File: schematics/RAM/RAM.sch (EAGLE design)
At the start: 31 parts

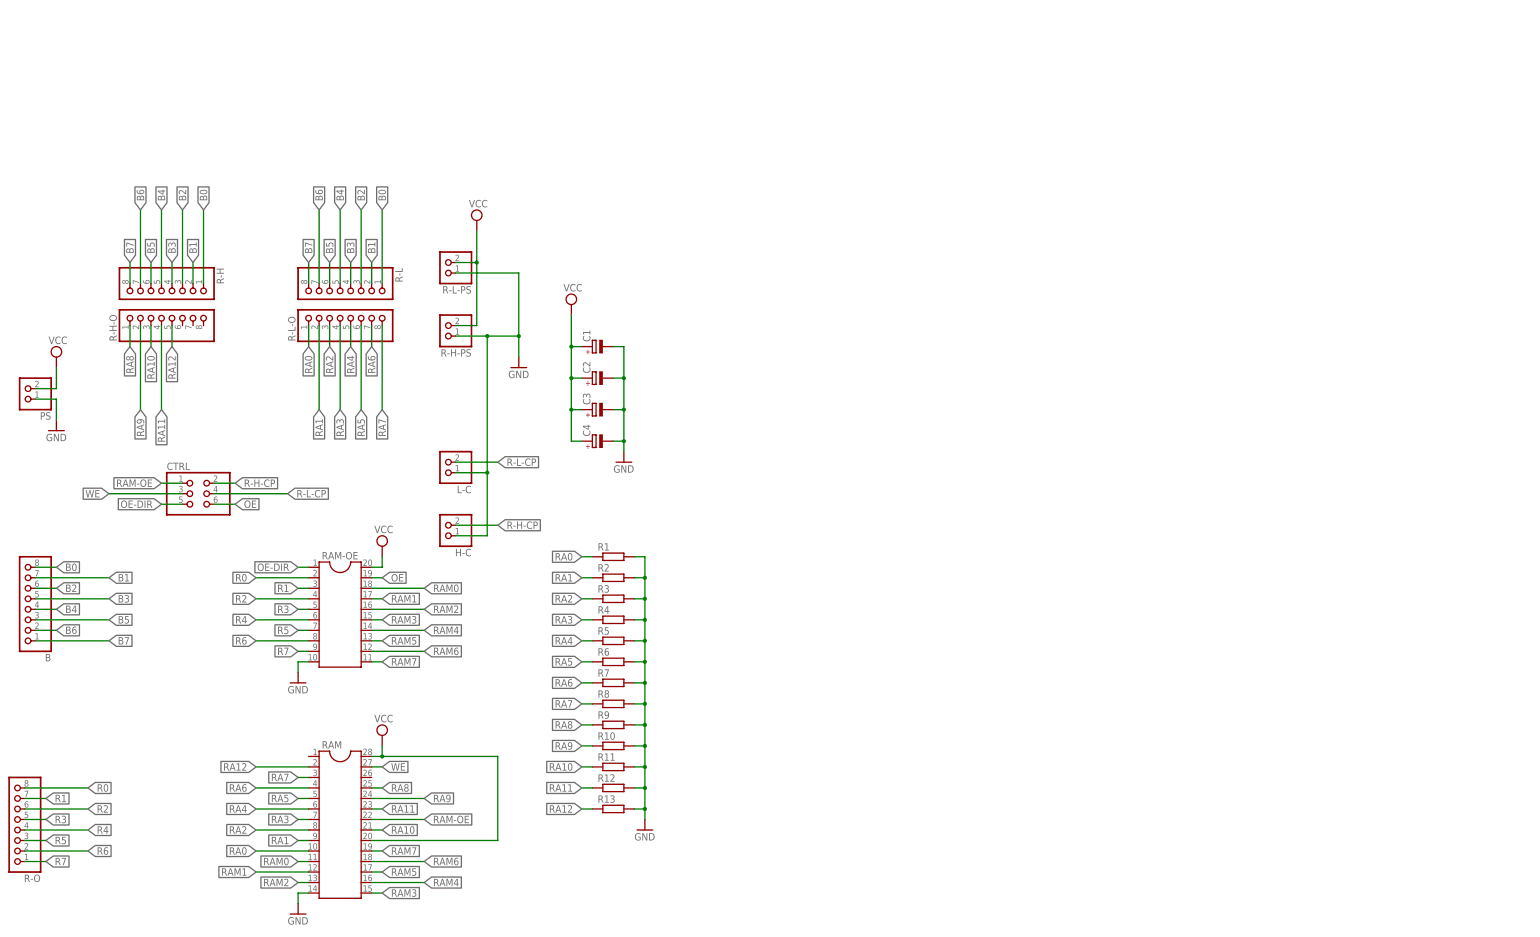
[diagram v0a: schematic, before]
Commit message: RAM merged with register.
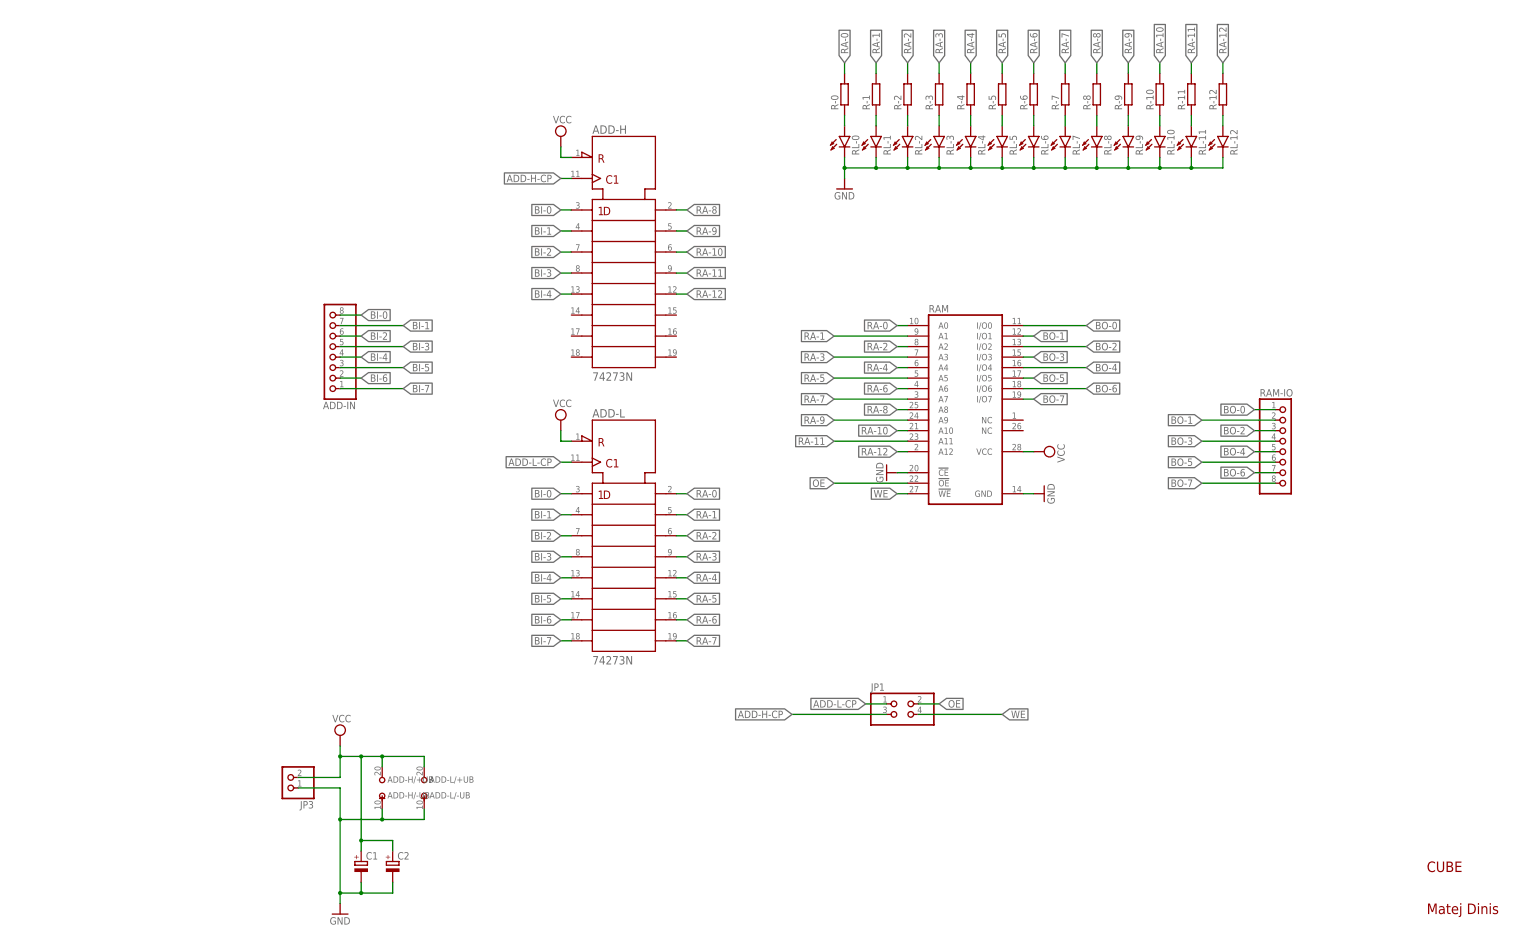
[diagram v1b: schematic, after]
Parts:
- removed B, R-H, R-H-O, R-L, R-L-O, R-O: (no value), pinhead:PINHD-1X8
- removed C3, C4: (no value), rcl:CPOL-EUE3.5-8
- removed CTRL: (no value), pinhead:PINHD-2X3
- removed H-C, L-C, PS, R-H-PS, R-L-PS: (no value), pinhead:PINHD-1X2
- removed R1, R10, R11, R12, R13, R2, R3, R4, R5, R6, R7, R8, R9: (no value), rcl:R-EU_0204/7
- removed RAM-OE: (no value), ic-package:DIL20S
- added ADD-H, ADD-L: 74273N, 74ttl-din:74273N
- added ADD-IN, RAM-IO: (no value), pinhead:PINHD-1X8
- added JP1: (no value), pinhead:PINHD-2X2
- added JP3: (no value), pinhead:PINHD-1X2
- added R-0, R-1, R-10, R-11, R-12, R-2, R-3, R-4, R-5, R-6, R-7, R-8, R-9: (no value), rcl:R-EU_0207/10
- added RL-0, RL-1, RL-10, RL-11, RL-12, RL-2, RL-3, RL-4, RL-5, RL-6, RL-7, RL-8, RL-9: (no value), led:LED5MM
- RAM: device ic-package:DIL28 -> memory-nec:28C64C
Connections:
- removed net B0: B.8, R-H.1, R-L.1
- removed net B1: B.7, R-H.2, R-L.2
- removed net B2: B.6, R-H.3, R-L.3
- removed net B3: B.5, R-H.4, R-L.4
- removed net B4: B.4, R-H.5, R-L.5
- removed net B5: B.3, R-H.6, R-L.6
- removed net B6: B.2, R-H.7, R-L.7
- removed net B7: B.1, R-H.8, R-L.8
- removed net OE-DIR: CTRL.5, RAM-OE.1
- removed net R-H-CP: CTRL.2, H-C.2
- removed net R-L-CP: CTRL.4, L-C.2
- removed net R0: R-O.8, RAM-OE.2
- removed net R1: R-O.7, RAM-OE.3
- removed net R2: R-O.6, RAM-OE.4
- removed net R3: R-O.5, RAM-OE.5
- removed net R4: R-O.4, RAM-OE.6
- removed net R5: R-O.3, RAM-OE.7
- removed net R6: R-O.2, RAM-OE.8
- removed net R7: R-O.1, RAM-OE.9
- removed net RA0: R-L-O.1, R1.1, RAM.10
- removed net RA1: R-L-O.2, R2.1, RAM.9
- removed net RA10: R-H-O.3, R11.1, RAM.21
- removed net RA11: R-H-O.4, R12.1, RAM.23
- removed net RA12: R-H-O.5, R13.1, RAM.2
- removed net RA2: R-L-O.3, R3.1, RAM.8
- removed net RA3: R-L-O.4, R4.1, RAM.7
- removed net RA4: R-L-O.5, R5.1, RAM.6
- removed net RA5: R-L-O.6, R6.1, RAM.5
- removed net RA6: R-L-O.7, R7.1, RAM.4
- removed net RA7: R-L-O.8, R8.1, RAM.3
- removed net RA8: R-H-O.1, R9.1, RAM.25
- removed net RA9: R-H-O.2, R10.1, RAM.24
- removed net RAM-OE: CTRL.1, RAM.22
- removed net RAM0: RAM-OE.18, RAM.11
- removed net RAM1: RAM-OE.17, RAM.12
- removed net RAM2: RAM-OE.16, RAM.13
- removed net RAM3: RAM-OE.15, RAM.15
- removed net RAM4: RAM-OE.14, RAM.16
- removed net RAM5: RAM-OE.13, RAM.17
- removed net RAM6: RAM-OE.12, RAM.18
- removed net RAM7: RAM-OE.11, RAM.19
- new net ADD-H-CP: ADD-H1.CLK, JP1.3
- new net ADD-L-CP: ADD-L1.CLK, JP1.1
- new net BI-0: ADD-H1.1D, ADD-IN.8, ADD-L1.1D
- new net BI-1: ADD-H1.2D, ADD-IN.7, ADD-L1.2D
- new net BI-2: ADD-H1.3D, ADD-IN.6, ADD-L1.3D
- new net BI-3: ADD-H1.4D, ADD-IN.5, ADD-L1.4D
- new net BI-4: ADD-H1.5D, ADD-IN.4, ADD-L1.5D
- new net BI-5: ADD-IN.3, ADD-L1.6D
- new net BI-6: ADD-IN.2, ADD-L1.7D
- new net BI-7: ADD-IN.1, ADD-L1.8D
- new net BO-0: RAM-IO.1, RAM.I/O0
- new net BO-1: RAM-IO.2, RAM.I/O1
- new net BO-2: RAM-IO.3, RAM.I/O2
- new net BO-3: RAM-IO.4, RAM.I/O3
- new net BO-4: RAM-IO.5, RAM.I/O4
- new net BO-5: RAM-IO.6, RAM.I/O5
- new net BO-6: RAM-IO.7, RAM.I/O6
- new net BO-7: RAM-IO.8, RAM.I/O7
- new net N$1: R-0.1, RL-0.A
- new net N$10: R-3.1, RL-3.A
- new net N$13: R-4.1, RL-4.A
- new net N$16: R-5.1, RL-5.A
- new net N$19: R-6.1, RL-6.A
- new net N$22: R-7.1, RL-7.A
- new net N$25: R-8.1, RL-8.A
- new net N$28: R-9.1, RL-9.A
- new net N$31: R-10.1, RL-10.A
- new net N$34: R-11.1, RL-11.A
- new net N$37: R-12.1, RL-12.A
- new net N$4: R-1.1, RL-1.A
- new net N$7: R-2.1, RL-2.A
- new net RA-0: ADD-L1.1Q, R-0.2, RAM.A0
- new net RA-1: ADD-L1.2Q, R-1.2, RAM.A1
- new net RA-10: ADD-H1.3Q, R-10.2, RAM.A10
- new net RA-11: ADD-H1.4Q, R-11.2, RAM.A11
- new net RA-12: ADD-H1.5Q, R-12.2, RAM.A12
- new net RA-2: ADD-L1.3Q, R-2.2, RAM.A2
- new net RA-3: ADD-L1.4Q, R-3.2, RAM.A3
- new net RA-4: ADD-L1.5Q, R-4.2, RAM.A4
- new net RA-5: ADD-L1.6Q, R-5.2, RAM.A5
- new net RA-6: ADD-L1.7Q, R-6.2, RAM.A6
- new net RA-7: ADD-L1.8Q, R-7.2, RAM.A7
- new net RA-8: ADD-H1.1Q, R-8.2, RAM.A8
- new net RA-9: ADD-H1.2Q, R-9.2, RAM.A9
- net GND: now also ADD-H/-UB.-UB, ADD-L/-UB.-UB, JP3.1, RAM.!CE, RAM.GND, RL-0.C, RL-1.C, RL-10.C, RL-11.C, RL-12.C, RL-2.C, RL-3.C, RL-4.C, RL-5.C, RL-6.C, RL-7.C, RL-8.C, RL-9.C; no longer C3.-, C4.-, H-C.1, L-C.1, PS.1, R-H-PS.1, R-L-PS.1, R1.2, R10.2, R11.2, R12.2, R13.2, R2.2, R3.2, R4.2, R5.2, R6.2, R7.2, R8.2, R9.2, RAM-OE.10, RAM.14
- net OE: now also JP1.2, RAM.!OE; no longer CTRL.6, RAM-OE.19
- net VCC: now also ADD-H/+UB.+UB, ADD-H1.!CLR, ADD-L/+UB.+UB, ADD-L1.!CLR, JP3.2, RAM.VCC; no longer C3.+, C4.+, PS.2, R-H-PS.2, R-L-PS.2, RAM-OE.20, RAM.20, RAM.28
- net WE: now also JP1.4, RAM.!WE; no longer CTRL.3, RAM.27
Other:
- note added: "CUBE"
- note added: "Matej Dinis"
- moved on the sheet: C1, C2
